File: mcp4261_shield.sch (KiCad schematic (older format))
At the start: 6 parts, among them P1 CONN_13, U1 MCP4261-PDIP, U2 MCP4261-PDIP

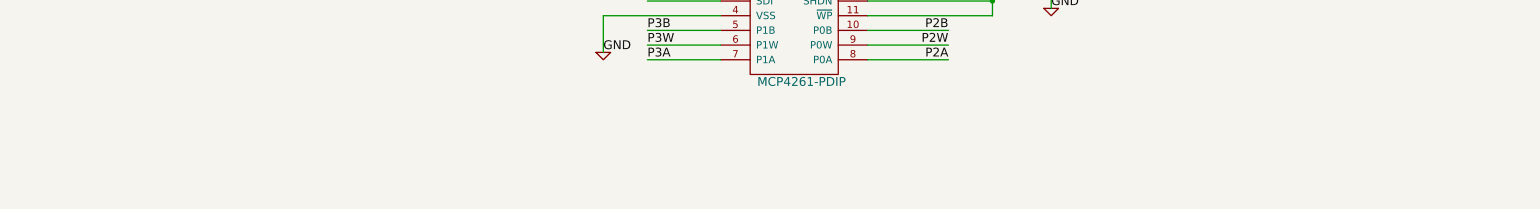
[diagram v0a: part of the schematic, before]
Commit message: Added svg and pdf of schematic.
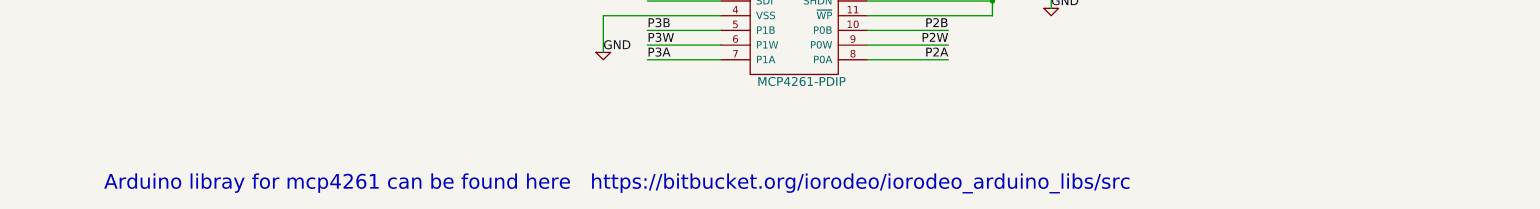
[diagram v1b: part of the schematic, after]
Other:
- note added: "Arduino libray for mcp4261 can be found here https://bitbucket.org/iorodeo/iorodeo_arduino_libs/src \n"
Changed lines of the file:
@@
-EESchema Schematic File Version 2  date Mon 24 Sep 2012 01:02:05 PM PDT
+EESchema Schematic File Version 2
 LIBS:power
 LIBS:device
@@
 LIBS:arduino
 LIBS:mcp4261_shield-cache
-EELAYER 25  0
+EELAYER 24 0
 EELAYER END
-$Descr A4 11700 8267
+$Descr A4 11693 8268
 encoding utf-8
 Sheet 1 1
@@
 F 0 "#PWR6" H 8950 2850 30  0001 C CNN
 F 1 "GND" H 8950 2780 30  0001 C CNN
+F 2 "" H 8950 2850 60  0001 C CNN
+F 3 "" H 8950 2850 60  0001 C CNN
 	1    8950 2850
 	1    0    0    -1
@@
 F 0 "P1" V 9810 2000 60  0000 C CNN
 F 1 "CONN_13" V 9920 2000 60  0000 C CNN
+F 2 "" H 9850 2000 60  0001 C CNN
+F 3 "" H 9850 2000 60  0001 C CNN
 	1    9850 2000
 	1    0    0    -1
@@
 F 0 "U2" H 6100 3900 60  0000 C CNN
 F 1 "MCP4261-PDIP" H 6350 3000 60  0000 C CNN
+F 2 "" H 6300 3450 60  0001 C CNN
+F 3 "" H 6300 3450 60  0001 C CNN
 	1    6300 3450
 	1    0    0    -1
@@
 F 0 "#PWR3" H 5000 3700 30  0001 C CNN
 F 1 "GND" H 5000 3630 30  0001 C CNN
+F 2 "" H 5000 3700 60  0001 C CNN
+F 3 "" H 5000 3700 60  0001 C CNN
 	1    5000 3700
 	1    0    0    -1
@@
 F 0 "C2" H 8100 3100 50  0000 L CNN
 F 1 "0.1uF" H 8100 2900 50  0000 L CNN
+F 2 "" H 8050 3000 60  0001 C CNN
+F 3 "" H 8050 3000 60  0001 C CNN
 	1    8050 3000
 	1    0    0    -1
@@
 F 0 "#PWR5" H 8050 3400 30  0001 C CNN
 F 1 "GND" H 8050 3330 30  0001 C CNN
+F 2 "" H 8050 3400 60  0001 C CNN
+F 3 "" H 8050 3400 60  0001 C CNN
 	1    8050 3400
 	1    0    0    -1
@@
 F 0 "#PWR4" H 8000 1750 30  0001 C CNN
 F 1 "GND" H 8000 1680 30  0001 C CNN
+F 2 "" H 8000 1750 60  0001 C CNN
+F 3 "" H 8000 1750 60  0001 C CNN
 	1    8000 1750
 	1    0    0    -1
@@
 F 0 "C1" H 8050 1450 50  0000 L CNN
 F 1 "0.1uF" H 8050 1250 50  0000 L CNN
+F 2 "" H 8000 1350 60  0001 C CNN
+F 3 "" H 8000 1350 60  0001 C CNN
 	1    8000 1350
 	1    0    0    -1
@@
 F 0 "#PWR2" H 4950 2050 30  0001 C CNN
 F 1 "GND" H 4950 1980 30  0001 C CNN
+F 2 "" H 4950 2050 60  0001 C CNN
+F 3 "" H 4950 2050 60  0001 C CNN
 	1    4950 2050
 	1    0    0    -1
@@
 F 0 "#FLG2" H 1550 1970 30  0001 C CNN
 F 1 "PWR_FLAG" H 1550 1930 30  0000 C CNN
+F 2 "" H 1550 1700 60  0001 C CNN
+F 3 "" H 1550 1700 60  0001 C CNN
 	1    1550 1700
 	1    0    0    -1
@@
 F 0 "#FLG1" H 1000 1970 30  0001 C CNN
 F 1 "PWR_FLAG" H 1000 1930 30  0000 C CNN
+F 2 "" H 1000 1700 60  0001 C CNN
+F 3 "" H 1000 1700 60  0001 C CNN
 	1    1000 1700
 	1    0    0    -1
@@
 F 0 "#PWR1" H 1000 2150 30  0001 C CNN
 F 1 "GND" H 1000 2080 30  0001 C CNN
+F 2 "" H 1000 2150 60  0001 C CNN
+F 3 "" H 1000 2150 60  0001 C CNN
 	1    1000 2150
 	1    0    0    -1
@@
 F 0 "U1" H 6050 2250 60  0000 C CNN
 F 1 "MCP4261-PDIP" H 6300 1350 60  0000 C CNN
+F 2 "" H 6250 1800 60  0001 C CNN
+F 3 "" H 6250 1800 60  0001 C CNN
 	1    6250 1800
 	1    0    0    -1
@@
 F 0 "SHIELD1" H 2550 3050 60  0000 C CNN
 F 1 "ARDUINO_SHIELD" H 2950 1150 60  0000 C CNN
+F 2 "" H 2900 2100 60  0001 C CNN
+F 3 "" H 2900 2100 60  0001 C CNN
 	1    2900 2100
 	1    0    0    -1
 $EndComp
+Text Notes 1600 4650 0    100  ~ 0
+Arduino libray for mcp4261 can be found here   https://bitbucket.org/iorodeo/iorodeo_arduino_libs/src   \n
 $EndSCHEMATC
